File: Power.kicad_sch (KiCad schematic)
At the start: 31 parts, among them IC2 LM66200DRLR, Q1 DMP3068L-7, SW8 SW_SPST, U3 MIC845H, U4 TPS631000DRLR, U5 MCP73831-2-OT

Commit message: Ratsnest organized
Certain pins on esp32 module changed to benefit layout. Named all decaps to dC. Current layout areas might be not optimal, i.e. complicated to wire
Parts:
- dC2: renamed from C2; footprint Capacitor_SMD:C_0805_2012Metric_Pad1.18x1.45mm_HandSolder -> Capacitor_SMD:C_0603_1608Metric_Pad1.08x0.95mm_HandSolder
- dC3: renamed from C3; footprint Capacitor_SMD:C_0805_2012Metric_Pad1.18x1.45mm_HandSolder -> Capacitor_SMD:C_0603_1608Metric_Pad1.08x0.95mm_HandSolder
- dC30: renamed from C30; footprint Capacitor_SMD:C_0805_2012Metric_Pad1.18x1.45mm_HandSolder -> Capacitor_SMD:C_0603_1608Metric_Pad1.08x0.95mm_HandSolder
- dC31: renamed from C31; footprint Capacitor_SMD:C_0805_2012Metric_Pad1.18x1.45mm_HandSolder -> Capacitor_SMD:C_0603_1608Metric_Pad1.08x0.95mm_HandSolder
- dC4: renamed from C4; footprint Capacitor_SMD:C_0805_2012Metric_Pad1.18x1.45mm_HandSolder -> Capacitor_SMD:C_0603_1608Metric_Pad1.08x0.95mm_HandSolder
- dC5: renamed from C5; footprint Capacitor_SMD:C_0805_2012Metric_Pad1.18x1.45mm_HandSolder -> Capacitor_SMD:C_0603_1608Metric_Pad1.08x0.95mm_HandSolder
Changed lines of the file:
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@@
 		(on_board yes)
 		(dnp no)
-		(property "Reference" "C3"
+		(property "Reference" "dC3"
 			(at 25.654 105.664 0)
 			(effects
@@
 			)
 		)
-		(property "Footprint" "Capacitor_SMD:C_0805_2012Metric_Pad1.18x1.45mm_HandSolder"
+		(property "Footprint" "Capacitor_SMD:C_0603_1608Metric_Pad1.08x0.95mm_HandSolder"
 			(at 20.6248 102.87 0)
 			(effects
@@
 			(project "Media Player"
 				(path "/5c19345b-3707-4c90-b593-78a9c3e56866/17b36465-6639-4c30-8d5f-ef2acae7afbe"
-					(reference "C3")
+					(reference "dC3")
 					(unit 1)
 				)
@@
 		(on_board yes)
 		(dnp no)
-		(property "Reference" "C30"
+		(property "Reference" "dC30"
 			(at 170.688 121.92 0)
 			(effects
@@
 			)
 		)
-		(property "Footprint" "Capacitor_SMD:C_0805_2012Metric_Pad1.18x1.45mm_HandSolder"
+		(property "Footprint" "Capacitor_SMD:C_0603_1608Metric_Pad1.08x0.95mm_HandSolder"
 			(at 176.53 123.19 0)
 			(effects
@@
 			(project "Media Player"
 				(path "/5c19345b-3707-4c90-b593-78a9c3e56866/17b36465-6639-4c30-8d5f-ef2acae7afbe"
-					(reference "C30")
+					(reference "dC30")
 					(unit 1)
 				)
@@
 		(on_board yes)
 		(dnp no)
-		(property "Reference" "C2"
+		(property "Reference" "dC2"
 			(at 105.664 44.704 0)
 			(effects
@@
 			)
 		)
-		(property "Footprint" "Capacitor_SMD:C_0805_2012Metric_Pad1.18x1.45mm_HandSolder"
+		(property "Footprint" "Capacitor_SMD:C_0603_1608Metric_Pad1.08x0.95mm_HandSolder"
 			(at 100.6348 41.91 0)
 			(effects
@@
 			(project "Media Player"
 				(path "/5c19345b-3707-4c90-b593-78a9c3e56866/17b36465-6639-4c30-8d5f-ef2acae7afbe"
-					(reference "C2")
+					(reference "dC2")
 					(unit 1)
 				)
@@
 		(on_board yes)
 		(dnp no)
-		(property "Reference" "C4"
+		(property "Reference" "dC4"
 			(at 39.624 105.664 0)
 			(effects
@@
 			)
 		)
-		(property "Footprint" "Capacitor_SMD:C_0805_2012Metric_Pad1.18x1.45mm_HandSolder"
+		(property "Footprint" "Capacitor_SMD:C_0603_1608Metric_Pad1.08x0.95mm_HandSolder"
 			(at 34.5948 102.87 0)
 			(effects
@@
 			(project "Media Player"
 				(path "/5c19345b-3707-4c90-b593-78a9c3e56866/17b36465-6639-4c30-8d5f-ef2acae7afbe"
-					(reference "C4")
+					(reference "dC4")
 					(unit 1)
 				)
@@
 		(on_board yes)
 		(dnp no)
-		(property "Reference" "C31"
+		(property "Reference" "dC31"
 			(at 92.964 44.704 0)
 			(effects
@@
 			)
 		)
-		(property "Footprint" "Capacitor_SMD:C_0805_2012Metric_Pad1.18x1.45mm_HandSolder"
+		(property "Footprint" "Capacitor_SMD:C_0603_1608Metric_Pad1.08x0.95mm_HandSolder"
 			(at 87.9348 41.91 0)
 			(effects
@@
 			(project "Media Player"
 				(path "/5c19345b-3707-4c90-b593-78a9c3e56866/17b36465-6639-4c30-8d5f-ef2acae7afbe"
-					(reference "C31")
+					(reference "dC31")
 					(unit 1)
 				)
@@
 		(on_board yes)
 		(dnp no)
-		(property "Reference" "C5"
+		(property "Reference" "dC5"
 			(at 253.492 125.476 0)
 			(effects
@@
 			)
 		)
-		(property "Footprint" "Capacitor_SMD:C_0805_2012Metric_Pad1.18x1.45mm_HandSolder"
+		(property "Footprint" "Capacitor_SMD:C_0603_1608Metric_Pad1.08x0.95mm_HandSolder"
 			(at 252.73 123.19 0)
 			(effects
@@
 			(project "Media Player"
 				(path "/5c19345b-3707-4c90-b593-78a9c3e56866/17b36465-6639-4c30-8d5f-ef2acae7afbe"
-					(reference "C5")
+					(reference "dC5")
 					(unit 1)
 				)

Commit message: Small Change to USB routing
Removed 0 resistors and change components to match reference schematic
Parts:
- added D7: RED, LED_SMD:LED_0603_1608Metric, symbol Device:LED
- added R12: 5.1kΩ, Resistor_SMD:R_0805_2012Metric, symbol Device:R_Small_US
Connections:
- net +3.3V: now also R12.1
- net GND: now also D7.1 (K)
- new net: D7.2 (A), R12.2
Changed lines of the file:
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@@
 	)
 	(junction
+		(at 266.7 116.84)
+		(diameter 0)
+		(color 0 0 0 0)
+	)
+	(junction
 		(at 21.59 60.96)
 		(diameter 0)
@@
 	(wire
 		(pts
+			(xy 266.7 138.43) (xy 266.7 137.16)
+		)
+		(stroke
+			(width 0)
+			(type default)
+		)
+	)
+	(wire
+		(pts
 			(xy 123.19 105.41) (xy 128.27 105.41)
 		)
@@
 	(wire
 		(pts
+			(xy 266.7 125.73) (xy 266.7 129.54)
+		)
+		(stroke
+			(width 0)
+			(type default)
+		)
+	)
+	(wire
+		(pts
 			(xy 149.86 26.67) (xy 149.86 33.02)
 		)
@@
 	(wire
 		(pts
+			(xy 266.7 116.84) (xy 266.7 120.65)
+		)
+		(stroke
+			(width 0)
+			(type default)
+		)
+	)
+	(wire
+		(pts
 			(xy 245.11 64.77) (xy 245.11 53.34)
 		)
@@
 	)
 	(symbol
+		(lib_id "Device:R_Small_US")
+		(at 266.7 123.19 0)
+		(unit 1)
+		(exclude_from_sim no)
+		(in_bom yes)
+		(on_board yes)
+		(dnp no)
+		(fields_autoplaced yes)
+		(property "Reference" "R12"
+			(at 269.24 121.9199 0)
+			(effects
+				(font
+					(size 1.27 1.27)
+				)
+				(justify left)
+			)
+		)
+		(property "Value" "5.1kΩ"
+			(at 269.24 124.4599 0)
+			(effects
+				(font
+					(size 1.27 1.27)
+				)
+				(justify left)
+			)
+		)
+		(property "Footprint" "Resistor_SMD:R_0805_2012Metric"
+			(at 266.7 123.19 0)
+			(effects
+				(font
+					(size 1.27 1.27)
+				)
+				(hide yes)
+			)
+		)
+		(property "Datasheet" "~"
+			(at 266.7 123.19 0)
+			(effects
+				(font
+					(size 1.27 1.27)
+				)
+				(hide yes)
+			)
+		)
+		(property "Description" "Resistor, small US symbol"
+			(at 266.7 123.19 0)
+			(effects
+				(font
+					(size 1.27 1.27)
+				)
+				(hide yes)
+			)
+		)
+		(pin "2"
+		)
+		(pin "1"
+		)
+		(instances
+			(project "Media Player"
+				(path "/5c19345b-3707-4c90-b593-78a9c3e56866/17b36465-6639-4c30-8d5f-ef2acae7afbe"
+					(reference "R12")
+					(unit 1)
+				)
+			)
+		)
+	)
+	(symbol
 		(lib_id "power:GND")
 		(at 252.73 138.43 0)
@@
 	)
 	(symbol
+		(lib_id "power:GND")
+		(at 266.7 138.43 0)
+		(unit 1)
+		(exclude_from_sim no)
+		(in_bom yes)
+		(on_board yes)
+		(dnp no)
+		(fields_autoplaced yes)
+		(property "Reference" "#PWR03"
+			(at 266.7 144.78 0)
+			(effects
+				(font
+					(size 1.27 1.27)
+				)
+				(hide yes)
+			)
+		)
+		(property "Value" "GND"
+			(at 266.7 143.51 0)
+			(effects
+				(font
+					(size 1.27 1.27)
+				)
+			)
+		)
+		(property "Footprint" ""
+			(at 266.7 138.43 0)
+			(effects
+				(font
+					(size 1.27 1.27)
+				)
+				(hide yes)
+			)
+		)
+		(property "Datasheet" ""
+			(at 266.7 138.43 0)
+			(effects
+				(font
+					(size 1.27 1.27)
+				)
+				(hide yes)
+			)
+		)
+		(property "Description" "Power symbol creates a global label with name \"GND\" , ground"
+			(at 266.7 138.43 0)
+			(effects
+				(font
+					(size 1.27 1.27)
+				)
+				(hide yes)
+			)
+		)
+		(pin "1"
+		)
+		(instances
+			(project "Media Player"
+				(path "/5c19345b-3707-4c90-b593-78a9c3e56866/17b36465-6639-4c30-8d5f-ef2acae7afbe"
+					(reference "#PWR03")
+					(unit 1)
+				)
+			)
+		)
+	)
+	(symbol
 		(lib_id "Device:R_Small_US")
 		(at 140.97 114.3 0)
@@
 					(unit 1)
 				)
+			)
+		)
+	)
+	(symbol
+		(lib_id "Device:LED")
+		(at 266.7 133.35 90)
+		(unit 1)
+		(exclude_from_sim no)
+		(in_bom yes)
+		(on_board yes)
+		(dnp no)
+		(fields_autoplaced yes)
+		(property "Reference" "D7"
+			(at 270.51 133.6674 90)
+			(effects
+				(font
+					(size 1.27 1.27)
+				)
+				(justify right)
+			)
+		)
+		(property "Value" "RED"
+			(at 270.51 136.2074 90)
+			(effects
+				(font
+					(size 1.27 1.27)
+				)
+				(justify right)
+			)
+		)
+		(property "Footprint" "LED_SMD:LED_0603_1608Metric"
+			(at 266.7 133.35 0)
+			(effects
+				(font
+					(size 1.27 1.27)
+				)
+				(hide yes)
+			)
+		)
+		(property "Datasheet" "~"
+			(at 266.7 133.35 0)
+			(effects
+				(font
+					(size 1.27 1.27)
+				)
+				(hide yes)
+			)
+		)
+		(property "Description" "Light emitting diode"
+			(at 266.7 133.35 0)
+			(effects
+				(font
+					(size 1.27 1.27)
+				)
+				(hide yes)
+			)
+		)
+		(property "Sim.Pins" "1=K 2=A"
+			(at 266.7 133.35 0)
+			(effects
+				(font
+					(size 1.27 1.27)
+				)
+				(hide yes)
+			)
+		)
+		(pin "2"
+		)
+		(pin "1"
+		)
+		(instances
+			(project ""
+				(path "/5c19345b-3707-4c90-b593-78a9c3e56866/17b36465-6639-4c30-8d5f-ef2acae7afbe"
+					(reference "D7")
+					(unit 1)
+				)

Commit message: Compacting part 1
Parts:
- renumbered BT1 to BT50, dC31 to C50, dC2 to C51, dC3 to C52, dC4 to C53, dC30 to C54, dC5 to C55, D4 to D50, D7 to D51, L3 to L50, Q1 to Q50, R19 to R50, R14 to R51, R23 to R52, R13 to R53, R30 to R54, R29 to R55, R46 to R56, R17 to R57, R22 to R58, R21 to R59, R20 to R60, R16 to R61, R15 to R62, R12 to R63, SW8 to SW50, TP9 to TP50, TP10 to TP51, TP11 to TP52, U5 to U50, U3 to U51, IC2 to U52, U4 to U53

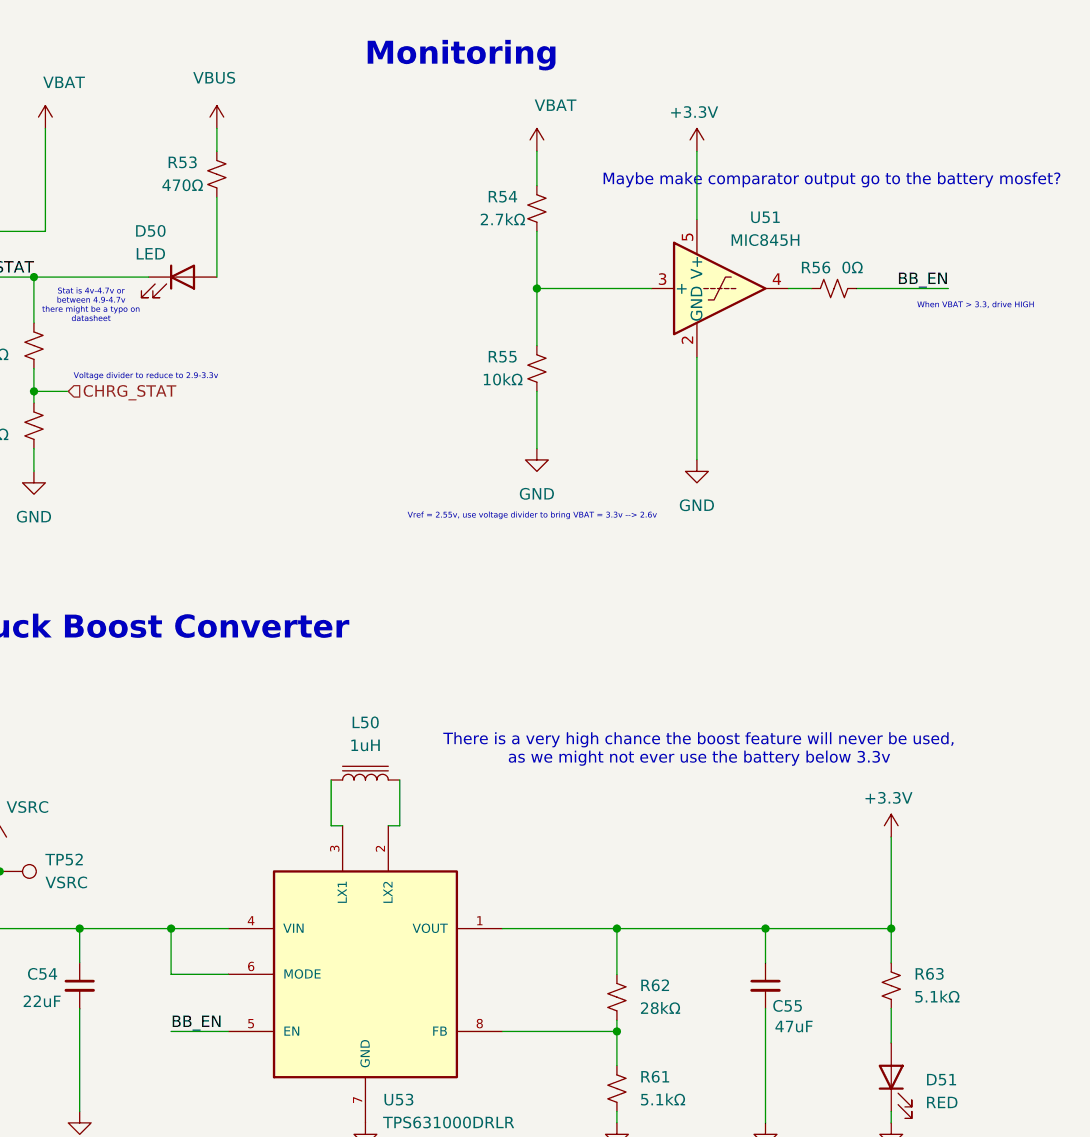
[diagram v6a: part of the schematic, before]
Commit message: Bucked
The Boost Buck Converter layout is from the datasheet. I'm not really sure how many via's I'll need for power since the IC is so small yet its the only source of power feeding all the other peripherals.
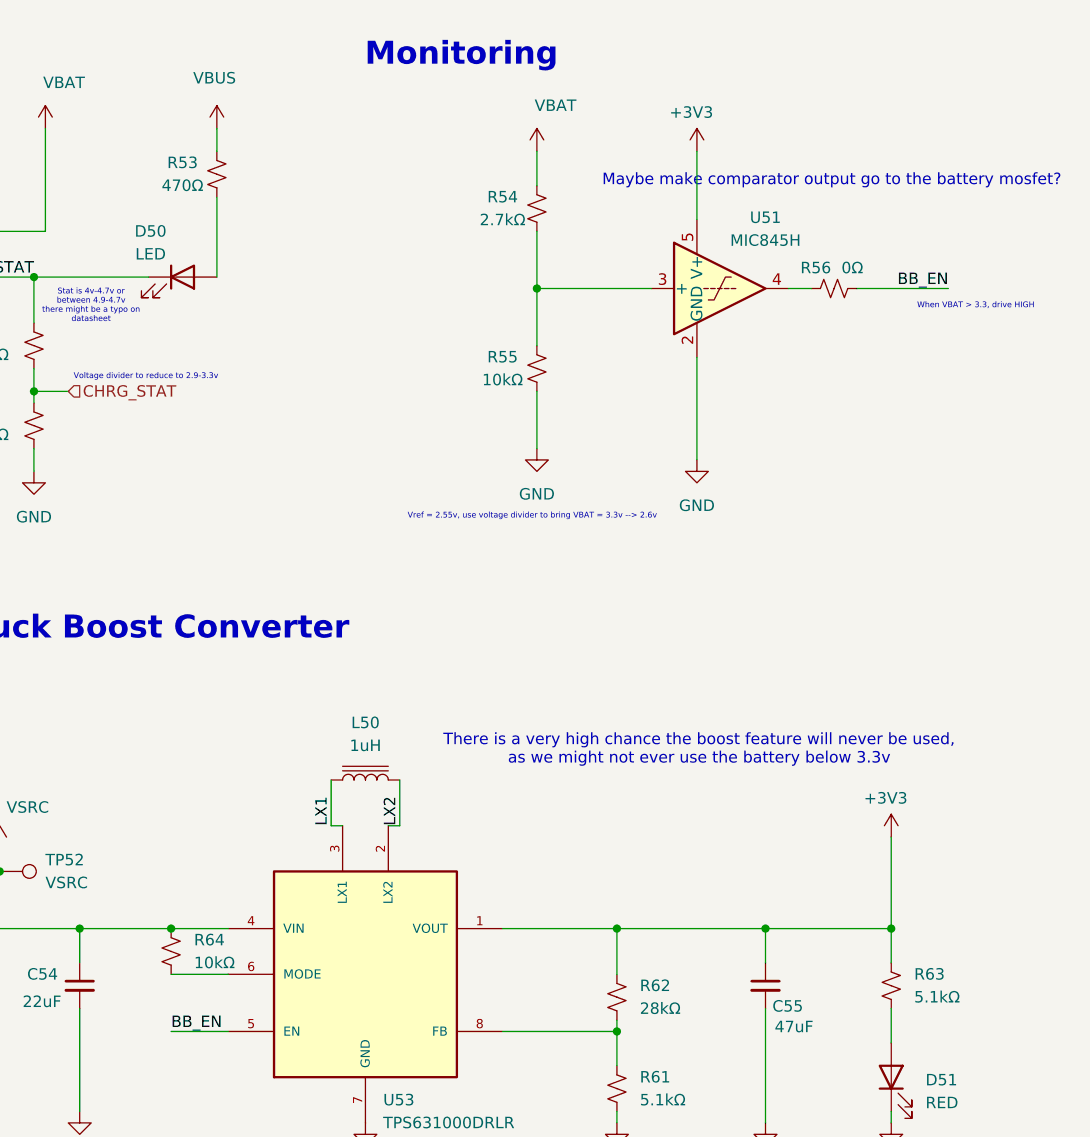
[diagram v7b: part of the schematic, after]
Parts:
- added R64: 10kΩ, Resistor_SMD:R_0603_1608Metric_Pad0.98x0.95mm_HandSolder, symbol Device:R_Small_US
- R50, R51, R52, R53, R54, R55, R56, R57, R58, R59, R60, R61, R62, R63: footprint Resistor_SMD:R_0805_2012Metric -> Resistor_SMD:R_0603_1608Metric_Pad0.98x0.95mm_HandSolder
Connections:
- net VSRC: now also R64.1; no longer U53.6 (MODE)
- net LX2: now reaches L50.2, U53.2 (LX2)
- net LX1: now reaches L50.1, U53.3 (LX1)
- net +3.3V renamed +3V3
- new net: R64.2, U53.6 (MODE)
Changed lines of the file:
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@@
 	)
 	(junction
-		(at 186.69 116.84)
+		(at 176.53 116.84)
 		(diameter 0)
 		(color 0 0 0 0)
 	)
 	(junction
-		(at 176.53 116.84)
+		(at 186.69 116.84)
 		(diameter 0)
 		(color 0 0 0 0)
@@
 	(wire
 		(pts
-			(xy 186.69 116.84) (xy 186.69 121.92)
-		)
-		(stroke
-			(width 0)
-			(type default)
-		)
-	)
-	(wire
-		(pts
 			(xy 252.73 116.84) (xy 252.73 120.65)
 		)
@@
 	(wire
 		(pts
-			(xy 34.29 31.75) (xy 41.91 31.75)
+			(xy 186.69 116.84) (xy 193.04 116.84)
 		)
 		(stroke
@@
 	(wire
 		(pts
-			(xy 186.69 116.84) (xy 193.04 116.84)
+			(xy 34.29 31.75) (xy 41.91 31.75)
 		)
 		(stroke
@@
 		)
 	)
+	(label "LX2"
+		(at 212.09 105.41 90)
+		(effects
+			(font
+				(size 1.27 1.27)
+			)
+			(justify left bottom)
+		)
+	)
+	(label "LX1"
+		(at 204.47 105.41 90)
+		(effects
+			(font
+				(size 1.27 1.27)
+			)
+			(justify left bottom)
+		)
+	)
 	(hierarchical_label "CHRG_STAT"
 		(shape input)
@@
 			)
 		)
-		(property "Footprint" "Resistor_SMD:R_0805_2012Metric"
+		(property "Footprint" "Resistor_SMD:R_0603_1608Metric_Pad0.98x0.95mm_HandSolder"
 			(at 266.7 123.19 0)
 			(effects
@@
 			)
 		)
-		(property "Footprint" "Resistor_SMD:R_0805_2012Metric"
+		(property "Footprint" "Resistor_SMD:R_0603_1608Metric_Pad0.98x0.95mm_HandSolder"
 			(at 260.35 45.72 0)
 			(effects
@@
 			)
 		)
-		(property "Footprint" "Resistor_SMD:R_0805_2012Metric"
+		(property "Footprint" "Resistor_SMD:R_0603_1608Metric_Pad0.98x0.95mm_HandSolder"
 			(at 86.36 109.22 0)
 			(effects
@@
 			)
 		)
-		(property "Footprint" "Resistor_SMD:R_0805_2012Metric"
+		(property "Footprint" "Resistor_SMD:R_0603_1608Metric_Pad0.98x0.95mm_HandSolder"
 			(at 140.97 121.92 0)
 			(effects
@@
 			)
 		)
-		(property "Footprint" "Resistor_SMD:R_0805_2012Metric"
+		(property "Footprint" "Resistor_SMD:R_0603_1608Metric_Pad0.98x0.95mm_HandSolder"
 			(at 134.62 50.8 0)
 			(effects
@@
 			)
 		)
-		(property "Footprint" "Resistor_SMD:R_0805_2012Metric"
+		(property "Footprint" "Resistor_SMD:R_0603_1608Metric_Pad0.98x0.95mm_HandSolder"
 			(at 133.35 107.95 0)
 			(effects
@@
 			)
 		)
-		(property "Footprint" "Resistor_SMD:R_0805_2012Metric"
+		(property "Footprint" "Resistor_SMD:R_0603_1608Metric_Pad0.98x0.95mm_HandSolder"
 			(at 140.97 114.3 0)
 			(effects
@@
 			)
 		)
-		(property "Footprint" "Resistor_SMD:R_0805_2012Metric"
+		(property "Footprint" "Resistor_SMD:R_0603_1608Metric_Pad0.98x0.95mm_HandSolder"
 			(at 191.77 33.02 0)
 			(effects
@@
 			)
 		)
-		(property "Footprint" "Resistor_SMD:R_0805_2012Metric"
+		(property "Footprint" "Resistor_SMD:R_0603_1608Metric_Pad0.98x0.95mm_HandSolder"
 			(at 236.22 124.46 0)
 			(effects
@@
 			)
 		)
-		(property "Footprint" "Resistor_SMD:R_0805_2012Metric"
+		(property "Footprint" "Resistor_SMD:R_0603_1608Metric_Pad0.98x0.95mm_HandSolder"
 			(at 227.33 36.83 0)
 			(effects
@@
 			)
 		)
-		(property "Footprint" "Resistor_SMD:R_0805_2012Metric"
+		(property "Footprint" "Resistor_SMD:R_0603_1608Metric_Pad0.98x0.95mm_HandSolder"
 			(at 236.22 134.62 0)
 			(effects
@@
 	)
 	(symbol
+		(lib_id "Device:R_Small_US")
+		(at 186.69 119.38 0)
+		(unit 1)
+		(exclude_from_sim no)
+		(in_bom yes)
+		(on_board yes)
+		(dnp no)
+		(fields_autoplaced yes)
+		(property "Reference" "R64"
+			(at 189.23 118.1099 0)
+			(effects
+				(font
+					(size 1.27 1.27)
+				)
+				(justify left)
+			)
+		)
+		(property "Value" "10kΩ"
+			(at 189.23 120.6499 0)
+			(effects
+				(font
+					(size 1.27 1.27)
+				)
+				(justify left)
+			)
+		)
+		(property "Footprint" "Resistor_SMD:R_0603_1608Metric_Pad0.98x0.95mm_HandSolder"
+			(at 186.69 119.38 0)
+			(effects
+				(font
+					(size 1.27 1.27)
+				)
+				(hide yes)
+			)
+		)
+		(property "Datasheet" "~"
+			(at 186.69 119.38 0)
+			(effects
+				(font
+					(size 1.27 1.27)
+				)
+				(hide yes)
+			)
+		)
+		(property "Description" "Resistor, small US symbol"
+			(at 186.69 119.38 0)
+			(effects
+				(font
+					(size 1.27 1.27)
+				)
+				(hide yes)
+			)
+		)
+		(pin "2"
+		)
+		(pin "1"
+		)
+		(instances
+			(project "Media Player"
+				(path "/5c19345b-3707-4c90-b593-78a9c3e56866/17b36465-6639-4c30-8d5f-ef2acae7afbe"
+					(reference "R64")
+					(unit 1)
+				)
+			)
+		)
+	)
+	(symbol
 		(lib_id "power:GND")
 		(at 149.86 64.77 0)
@@
 			)
 		)
-		(property "Footprint" "Resistor_SMD:R_0805_2012Metric"
+		(property "Footprint" "Resistor_SMD:R_0603_1608Metric_Pad0.98x0.95mm_HandSolder"
 			(at 166.37 52.07 0)
 			(effects
@@
 			)
 		)
-		(property "Footprint" "Resistor_SMD:R_0805_2012Metric"
+		(property "Footprint" "Resistor_SMD:R_0603_1608Metric_Pad0.98x0.95mm_HandSolder"
 			(at 227.33 54.61 0)
 			(effects
@@
 			)
 		)
-		(property "Value" "+3.3V"
+		(property "Value" "+3V3"
 			(at 263.652 102.362 0)
 			(effects
@@
 			)
 		)
-		(property "Value" "+3.3V"
+		(property "Value" "+3V3"
 			(at 242.062 26.162 0)
 			(effects
@@
 			)
 		)
-		(property "Footprint" "Resistor_SMD:R_0805_2012Metric"
+		(property "Footprint" "Resistor_SMD:R_0603_1608Metric_Pad0.98x0.95mm_HandSolder"
 			(at 171.45 60.96 0)
 			(effects

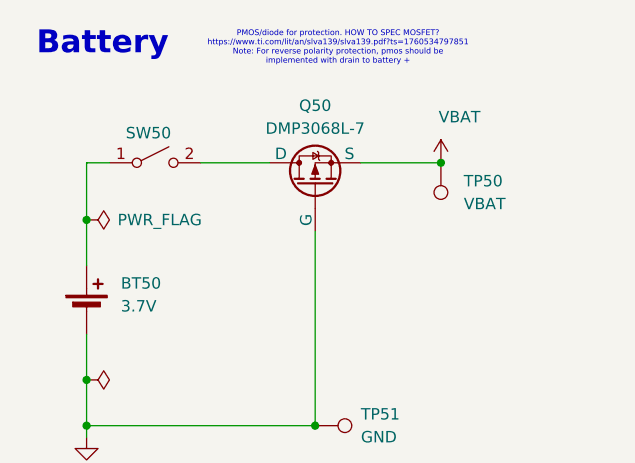
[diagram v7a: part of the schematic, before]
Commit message: Layout Draft 2, or almost
Charger layout based off of reference. Used more copper regions rather than traces. Other traces like buttons and test pads routed. Tried my best to make it all look good and parallel.

Added more silkscreen and logo.

STILL NEED TO DO POWER PLANE.
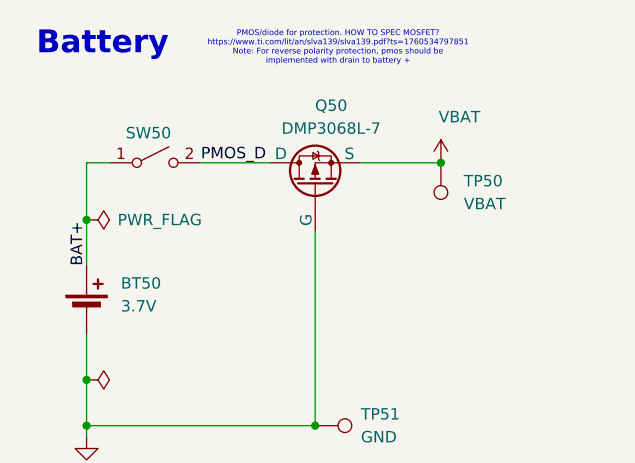
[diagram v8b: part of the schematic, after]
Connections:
- net BAT+: now reaches BT50.1 (+), SW50.1 (A)
- net PMOS_D: now reaches Q50.1 (D), SW50.2 (B)
